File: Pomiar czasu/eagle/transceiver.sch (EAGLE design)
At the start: 61 parts, among them IC1 MEGA8-AI, U1 RFM69HW

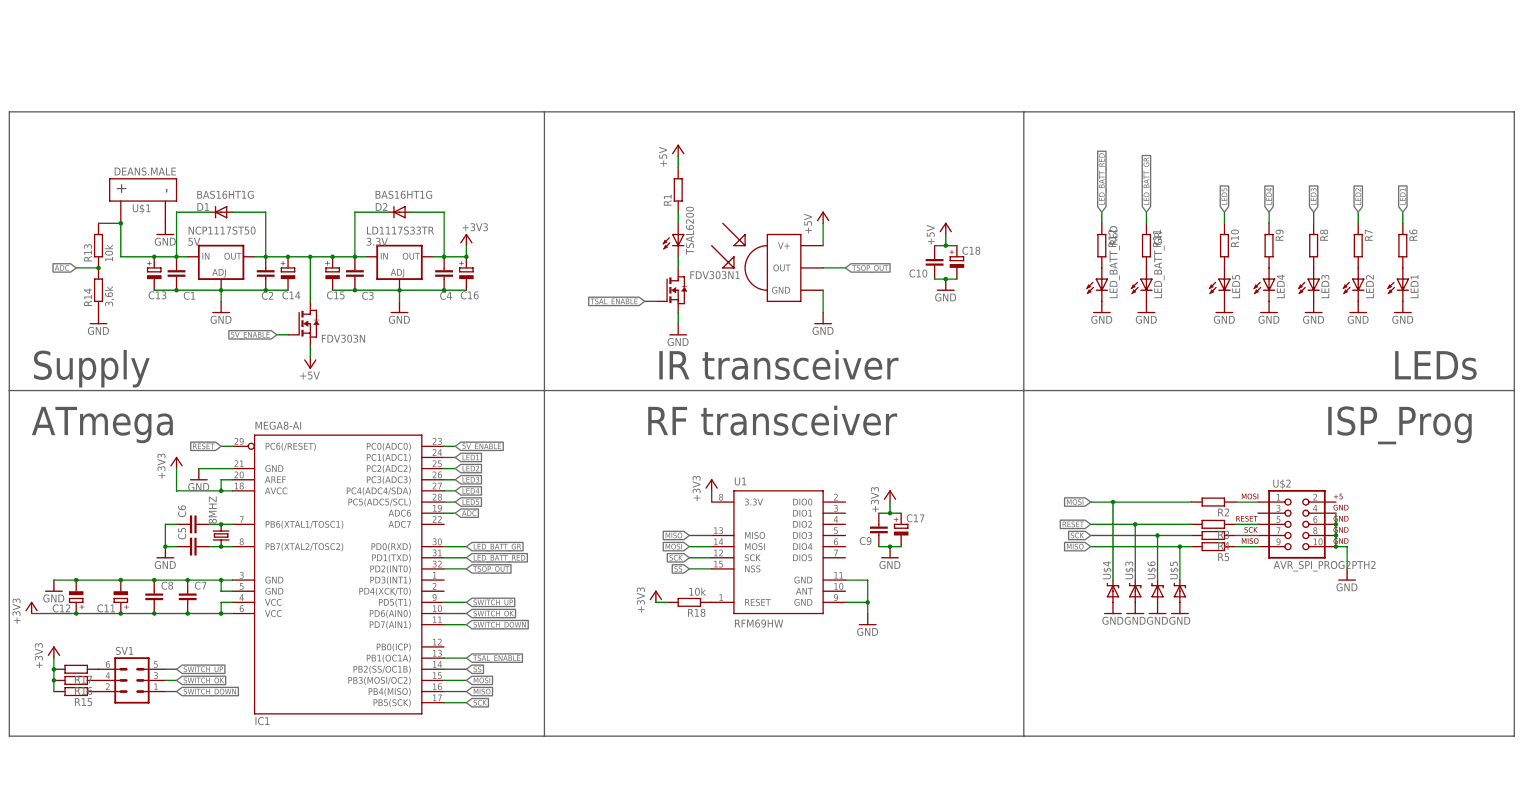
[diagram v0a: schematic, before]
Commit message: defines added, demo program
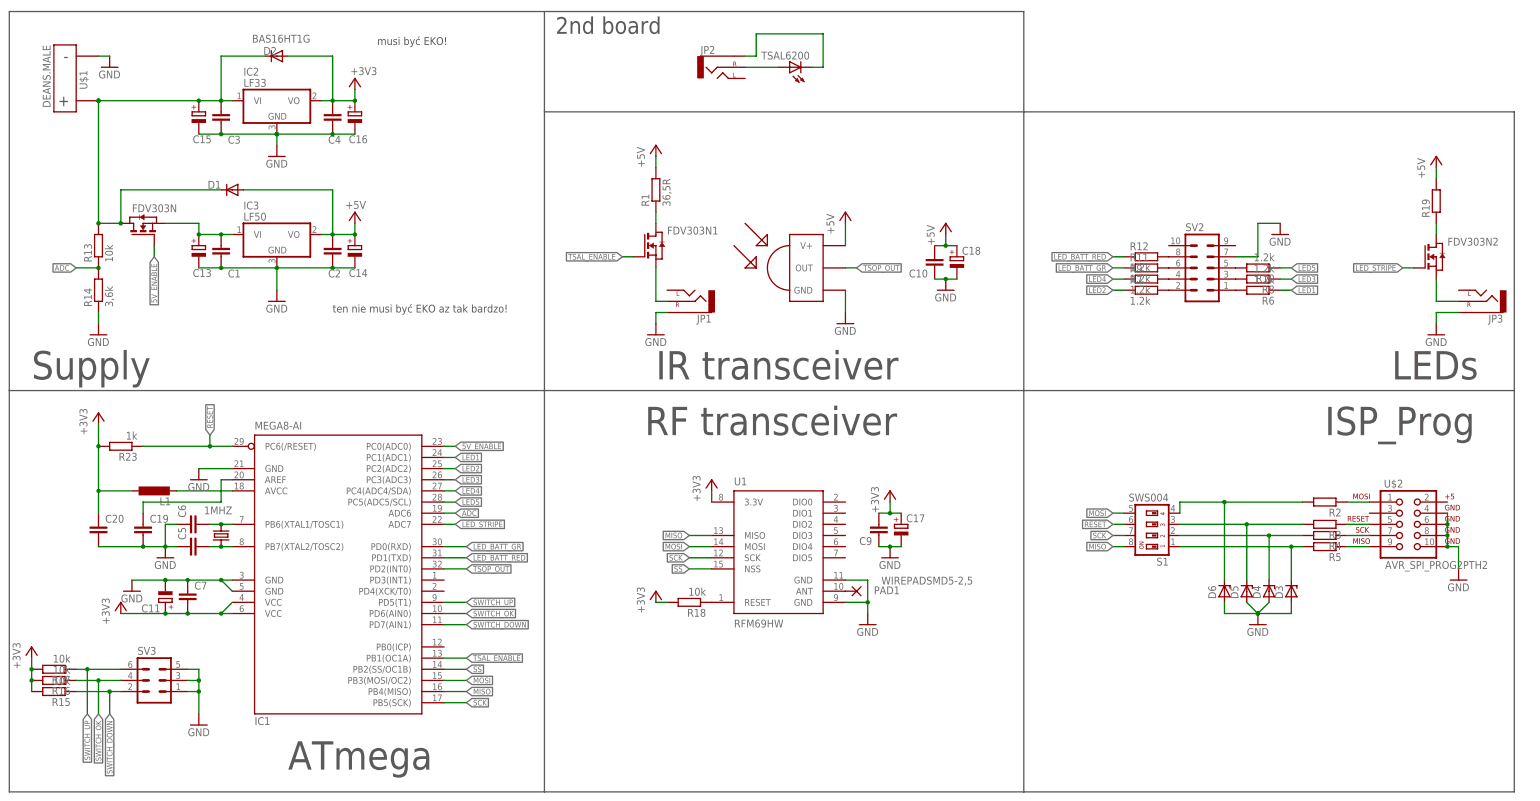
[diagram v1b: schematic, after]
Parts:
- removed C12: (no value), resistor:CPOL-EUE3.5-8
- removed C8: (no value), resistor:C-EUC0805
- removed LD1117S33TR: 3.3V, SparkFun-PowerIC:V_REG_317SMD
- removed LED1, LED2, LED3, LED4, LED5, LED_BATT_GR, LED_BATT_RED: (no value), led:LED5MM
- removed NCP1117ST50: 5V, SparkFun-PowerIC:V_REG_317SMD
- removed SV1: (no value), con-harting-ml:ML6
- removed U$3, U$4, U$5, U$6: DIODE-ZENER-BZT52, SparkFun:DIODE-ZENER-BZT52
- added C19, C20: (no value), resistor:C-EUC0805
- added D3, D4, D5, D6: (no value), diode:ZENER-DIODESOD80C
- added FDV303N2: (no value), zetex:NMOSSOT23
- added IC2: LF33, linear:7805DT
- added IC3: LF50, linear:7805DT
- added JP1, JP2, JP3: (no value), SparkFun-Connectors:AUDIO-JACKPTH
- added L1: (no value), resistor:L-EU0204V
- added PAD1: WIREPADSMD5-2,5, wirepad:WIREPADSMD5-2,5
- added R19: (no value), resistor:R-EU_R0805
- added R23: 1k, resistor:R-EU_R0805
- added S1: SWS004, smd-special:SWS004
- added SV2: (no value), con-harting-ml:ML10
- added SV3: (no value), con-harting-ml:ML6
- C11, C13, C14, C15, C16, C17, C18: device resistor:CPOL-EUE3.5-8 -> rcl:CPOL-EUE2.5-5
- R1: value (none) -> 36,5R
- R10, R12, R6, R7, R8, R9: value (none) -> 1.2k
- R11: value (none) -> 1,2k
- R15, R16, R17: value (none) -> 10k
- renumbered 8MHZ to 1MHZ
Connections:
- removed net GND: C1.2, C10.1, C11.-, C12.-, C13.-, C14.-, C15.-, C16.-, C17.-, C18.-, C2.2, C3.2, C4.2, C5.1, C6.1, C7.1, C8.1, C9.1, FDV303N1.S, IC1.GND, IC1.GND@1, IC1.GND@2, LD1117S33TR.ADJ, LED1.C, LED2.C, LED3.C, LED4.C, LED5.C, LED_BATT_GR.C, LED_BATT_RED.C, NCP1117ST50.ADJ, R14.1, TSOP.GND, U$1.P$NEG, U$2.10, U$2.4, U$2.6, U$2.8, U$3.A, U$4.A, U$5.A, U$6.A, U1.GND@1, U1.GND@2
- removed net N$18: R15.1, SV1.2
- removed net N$19: R16.1, SV1.4
- removed net N$20: R17.1, SV1.6
- new net $1S1: C1.2, C10.1, C11.-, C13.-, C14.-, C15.-, C16.-, C17.-, C18.-, C19.2, C2.2, C20.2, C3.2, C4.2, C5.1, C6.1, C7.1, C9.1, D3.A, D4.A, D5.A, D6.A, IC1.GND, IC1.GND@1, IC1.GND@2, IC2.GND, IC3.GND, JP1.SLEEVE, JP3.SLEEVE, R14.1, SV2.7, SV3.1, SV3.3, SV3.5, TSOP.GND, U$1.P$NEG, U$2.10, U$2.4, U$2.6, U$2.8, U1.GND@1, U1.GND@2
- new net LED_STRIPE: FDV303N2.G, IC1.ADC7
- new net N$22: JP2.SLEEVE, TSAL6200.C
- new net N$23: FDV303N1.S, JP1.RIGHT
- new net N$24: FDV303N2.S, JP3.RIGHT
- new net N$25: FDV303N2.D, R19.1
- new net N$26: C19.1, IC1.AREF
- new net N$27: C15.+, C3.1, D1.C, D2.C, FDV303N.D, IC2.VI, R13.2, U$1.P$POS
- new net N$28: PAD1.P, U1.ANT
- new net N$29: D6.C, R2.2, S1.4
- new net N$30: D5.C, R3.2, S1.3
- new net N$31: D4.C, R4.2, S1.2
- new net N$32: D3.C, R5.2, S1.1
- net +3V3: now also C20.1, IC2.VO, L1.1, R23.2; no longer C12.+, C8.2, IC1.AREF, IC1.AVCC, LD1117S33TR.OUT
- net +5V: now also C14.+, C2.1, D1.A, IC3.VO, R19.2; no longer FDV303N.S
- net MISO: now also S1.8; no longer R5.2, U$5.C
- net MOSI: now also S1.5; no longer R2.2, U$4.C
- net N$1: now also FDV303N.S, IC3.VI; no longer D1.C, NCP1117ST50.IN, R13.2, U$1.P$POS
- net N$10: now also SV2.2; no longer LED2.A
- net N$11: now also SV2.3; no longer LED3.A
- net N$12: now also SV2.4; no longer LED4.A
- net N$13: now also SV2.5; no longer LED5.A
- net N$16: now also SV2.6; no longer LED_BATT_GR.A
- net N$17: now also SV2.8; no longer LED_BATT_RED.A
- net N$2: now also IC1.AVCC, L1.2; no longer C14.+, C15.+, C2.1, C3.1, D1.A, D2.C, FDV303N.D, LD1117S33TR.IN, NCP1117ST50.OUT
- net N$3: now also JP2.RIGHT, TSAL6200.A; no longer FDV303N1.D, TSAL6200.C
- net N$8: now also FDV303N1.D; no longer TSAL6200.A
- net N$9: now also SV2.1; no longer LED1.A
- net RESET: now also R23.1, S1.6; no longer R3.2, U$3.C
- net SCK: now also S1.7; no longer R4.2, U$6.C
- net SWITCH_DOWN: now also R15.1, SV3.2; no longer SV1.1
- net SWITCH_OK: now also R16.1, SV3.4; no longer SV1.3
- net SWITCH_UP: now also R17.1, SV3.6; no longer SV1.5
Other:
- note added: "2nd board"
- note added: "musi być EKO!"
- note added: "ten nie musi być EKO az tak bardzo!"
- moved on the sheet: C1, C11, C13, C14, C15, C16, C2, C3, C4, D1, D2, FDV303N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

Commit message: ADC slave, master project  created
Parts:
- removed 1MHZ: (no value), crystal:CRYSTALHC49UP
- removed C5, C6: (no value), resistor:C-EUC0805
- added X1: (no value), con-phoenix-254:MPT2
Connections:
- removed net N$14: 1MHZ.2, C6.2, IC1.PB6(XTAL1/TOSC1)
- removed net N$15: 1MHZ.1, C5.2, IC1.PB7(XTAL2/TOSC2)
- new net N$19: U$1.P$POS, X1-2.1
- net $1S1: now also SV2.10, SV2.9; no longer C5.1, C6.1
- net LED_STRIPE: now also IC1.PB0(ICP); no longer IC1.ADC7
- net N$27: now also X1-1.1; no longer U$1.P$POS
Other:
- moved on the sheet: C1, C13, C14, C15, C16, C2, C3, C4, D1, D2, FDV303N, IC2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
